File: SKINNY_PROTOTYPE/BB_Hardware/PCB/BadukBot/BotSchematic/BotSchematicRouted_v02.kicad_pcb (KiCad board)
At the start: 2 copper layers, 93 x 22.5 mm, 90 parts, among them J1 MOLEX781710002, J10 A316DA2SV71, J11 62401621722, J12 A316DA2SV71, J13 0877601616, J2 MOLEX781710003, M1 Pos1a, M2 Neg1a, M3 Pos2a, M4 Neg2a, P1 SWDPads, P4 Conn01x02Female, P5 Pads, Q1 MMBT3904LT1G, Q2 MMBT3904LT1G, Q3 MMBT3904LT1G, Q4 MMBT3904LT1G, U1 STM32F051C8U6, U2 LSM6DS3, U3 A3901SEJTRT, U4 ADP122ACPZ33R7, U5 AT42QT1070MMHCTND, U6 MCP73831T2ACIOT, U7 NRF24L01PR7, Y1 7V16000MAAET

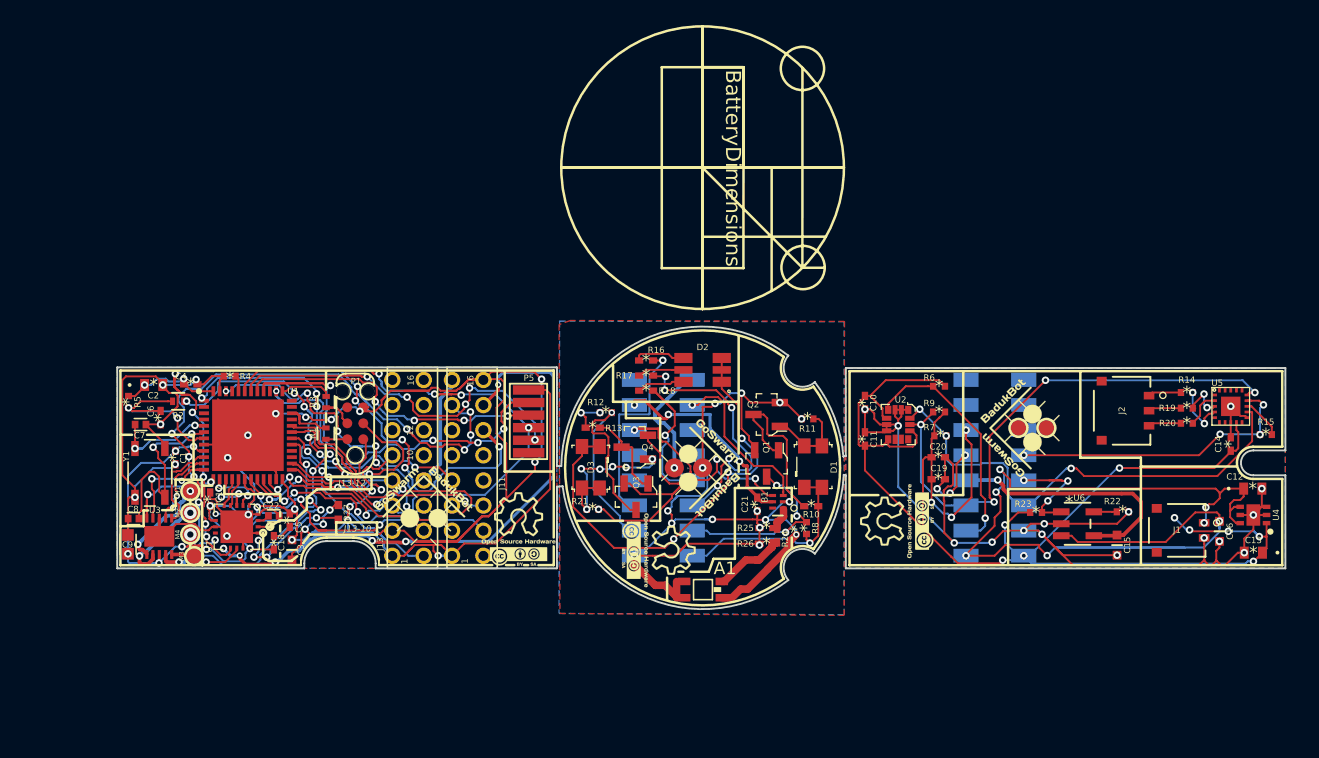
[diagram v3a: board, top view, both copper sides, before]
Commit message: Added images of the board; minor changes to BOM; Attempts to use KiCost to automate component shopping; Minor changes to copper pours on board
Working on getting KiCost to work with the xml generated by KiCAD to make shopping for parts easy at Octopart. Looks to be approx $20 per board
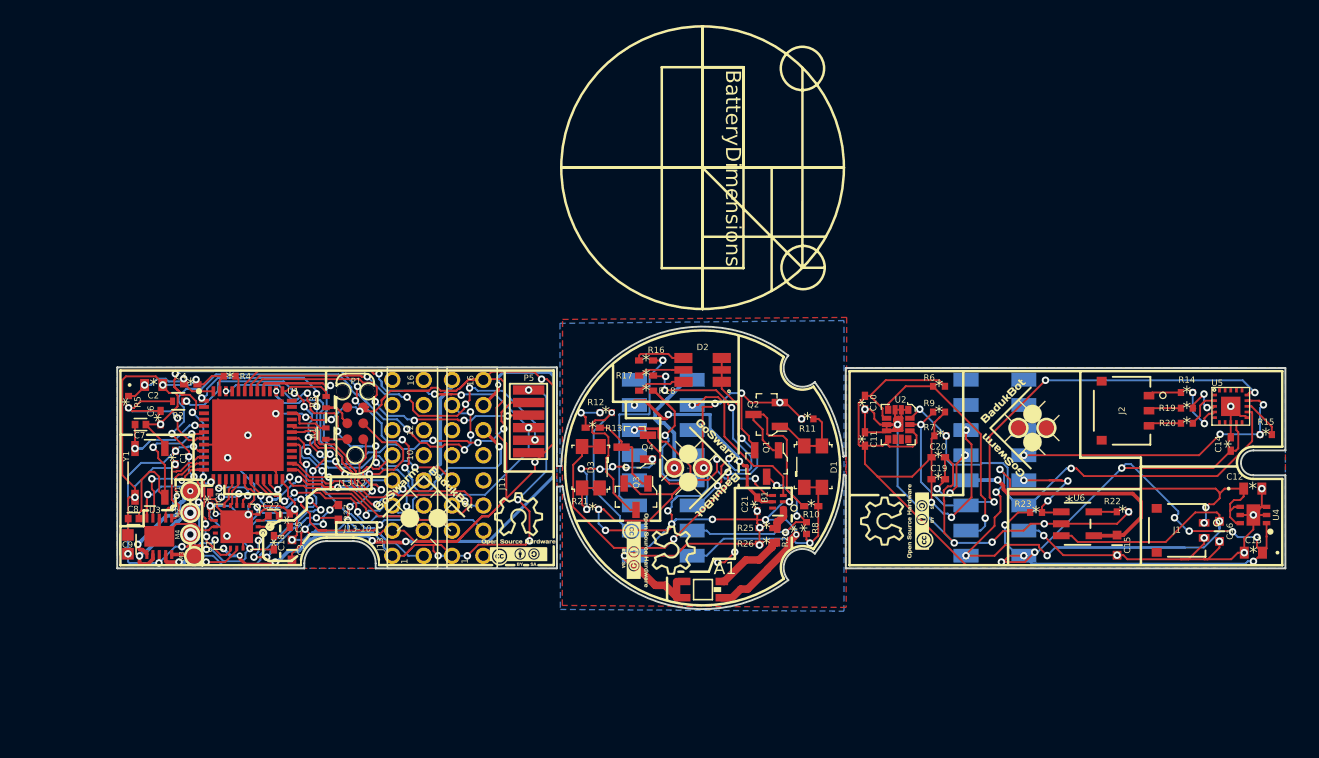
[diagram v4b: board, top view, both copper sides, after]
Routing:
- net 21a33v: track 0.00 -> 110.6 mm, vias 10 -> 11
- net 21a_3.3v: track 116.3 -> 13.7 mm
- net 2aGND: track 0.00 -> 77.1 mm, vias 17 -> 18
- net 23aGround: track 4.14 -> 73.4 mm, vias 16 -> 15
- net 2a_GND: track 97.5 -> 30.4 mm, vias 0 -> 2
- net 23a_Ground: track 91.6 -> 27.4 mm
- net 12bA1: track 64.9 -> 61.5 mm
- net (no net): track 0.00 -> 1.70 mm
- net 1b33v: track 121.6 -> 123.3 mm, vias 18 -> 22
- net 2bGND: track 167.9 -> 168.9 mm
- net 3bPHOTODIODE1: track 28.9 -> 28.3 mm
- net Net-(M1-Pad1): vias 3 -> 2
- added copper zone on B.Cu, net 23aGround
- removed copper zone on B.Cu, net 23a_Ground
